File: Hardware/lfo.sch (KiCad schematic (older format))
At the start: 51 parts, among them Q5 2N3904, Q6 2N3904, Q7 2N3904, Q8 2N3904, SW1 SW_DPDT_x2, U4 TL074

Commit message: fix some bias voltage issues in the LFO schematic. Also begin working on envelope firmware, but this is in progress.
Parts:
- added C?: 220uF, Capacitors_SMD:CP_Elec_8x10, symbol CP1
- added R?: 100k, digikey-footprints:0805, symbol R
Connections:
- net GND: now also R?.2
- net lfo_square: now also R?.1
- net at R75.1, R76.2, U4.1: now also C?.1; no longer R78.2
- new net: C?.2, R78.2
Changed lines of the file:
@@
 	3000 3100 2750 3100
 Wire Wire Line
-	2750 3600 2750 3100
+	2750 3100 2750 3600
 Connection ~ 2750 3600
 Wire Wire Line
 	2700 3850 2700 3800
 Wire Wire Line
-	1900 2100 1900 4250
+	1900 3050 1900 4250
 Wire Wire Line
 	1900 4250 1600 4250
@@
 Wire Wire Line
 	2300 2100 2300 2200
-Text Label 2500 2600 0    60   ~ 0
+Text Label 2700 2600 0    60   ~ 0
 lfo_square
 Wire Wire Line
-	2500 2600 2300 2600
+	2300 2600 2700 2600
 Connection ~ 2300 2600
 Text Label 4250 3700 0    60   ~ 0
@@
 	1    0    0    1
 $EndComp
+$Comp
+L R R?
+U 1 1 5C50BA99
+P 2550 2850
+F 0 "R?" V 2630 2850 50  0000 C CNN
+F 1 "100k" V 2550 2850 50  0000 C CNN
+F 2 "digikey-footprints:0805" V 2480 2850 50  0001 C CNN
+F 3 "" H 2550 2850 50  0001 C CNN
+	1    2550 2850
+	1    0    0    -1
+$EndComp
+Wire Wire Line
+	2550 2700 2550 2700
+Wire Wire Line
+	2550 2700 2550 2600
+Connection ~ 2550 2600
+$Comp
+L GND #PWR?
+U 1 1 5C50BC49
+P 2550 3000
+F 0 "#PWR?" H 2550 2750 50  0001 C CNN
+F 1 "GND" H 2550 2850 50  0000 C CNN
+F 2 "" H 2550 3000 50  0001 C CNN
+F 3 "" H 2550 3000 50  0001 C CNN
+	1    2550 3000
+	-1   0    0    -1
+$EndComp
+$Comp
+L CP1 C?
+U 1 1 5C50BEF7
+P 1900 2900
+F 0 "C?" H 1925 3000 50  0000 L CNN
+F 1 "220uF" H 1925 2800 50  0000 L CNN
+F 2 "Capacitors_SMD:CP_Elec_8x10" H 1900 2900 50  0001 C CNN
+F 3 "" H 1900 2900 50  0001 C CNN
+	1    1900 2900
+	-1   0    0    1
+$EndComp
+Wire Wire Line
+	1900 2750 1900 2100
 $EndSCHEMATC

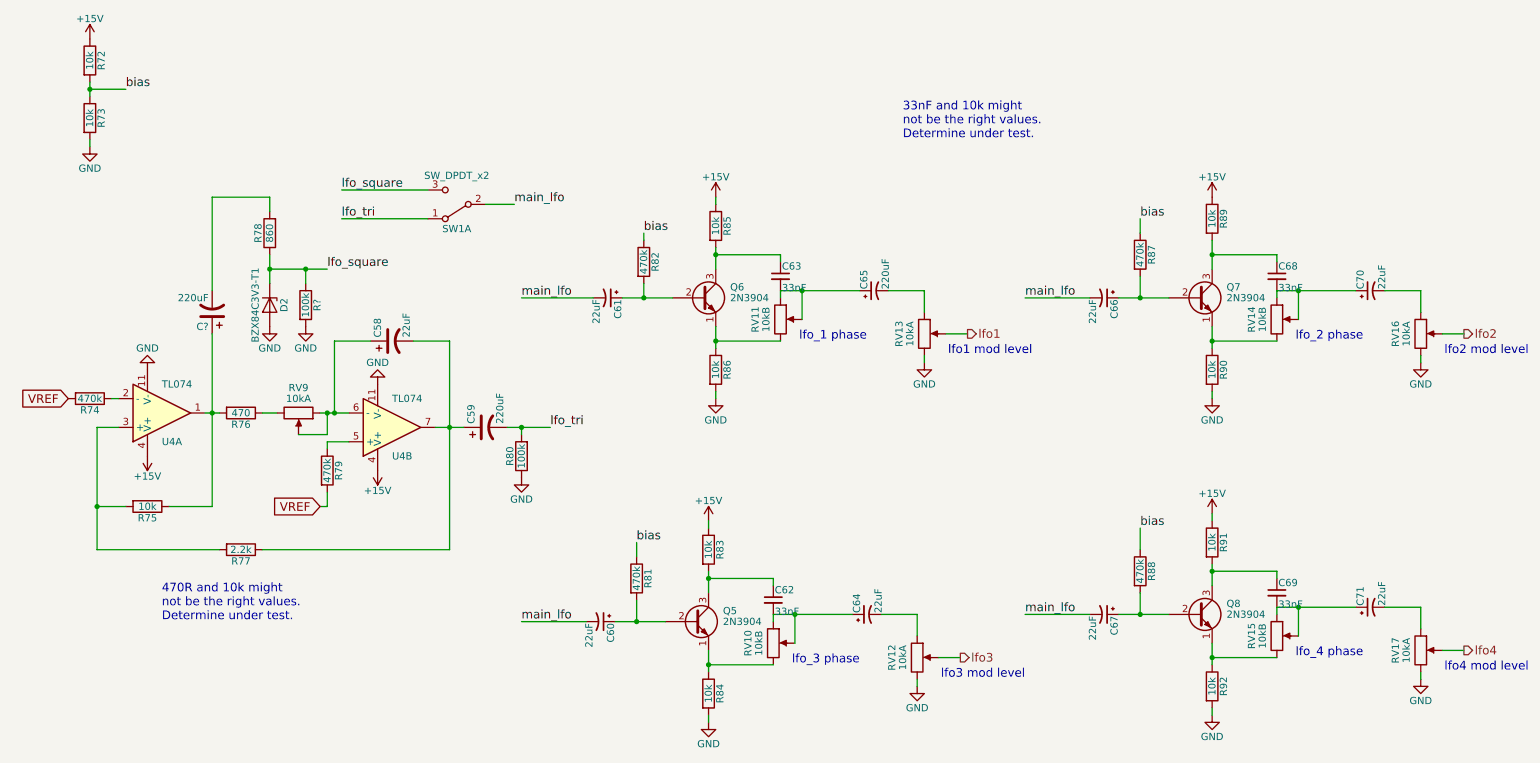
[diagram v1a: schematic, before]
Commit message: change 3.3V to 5V, fix LFO biasing, LPF, JFET bias trim pots.
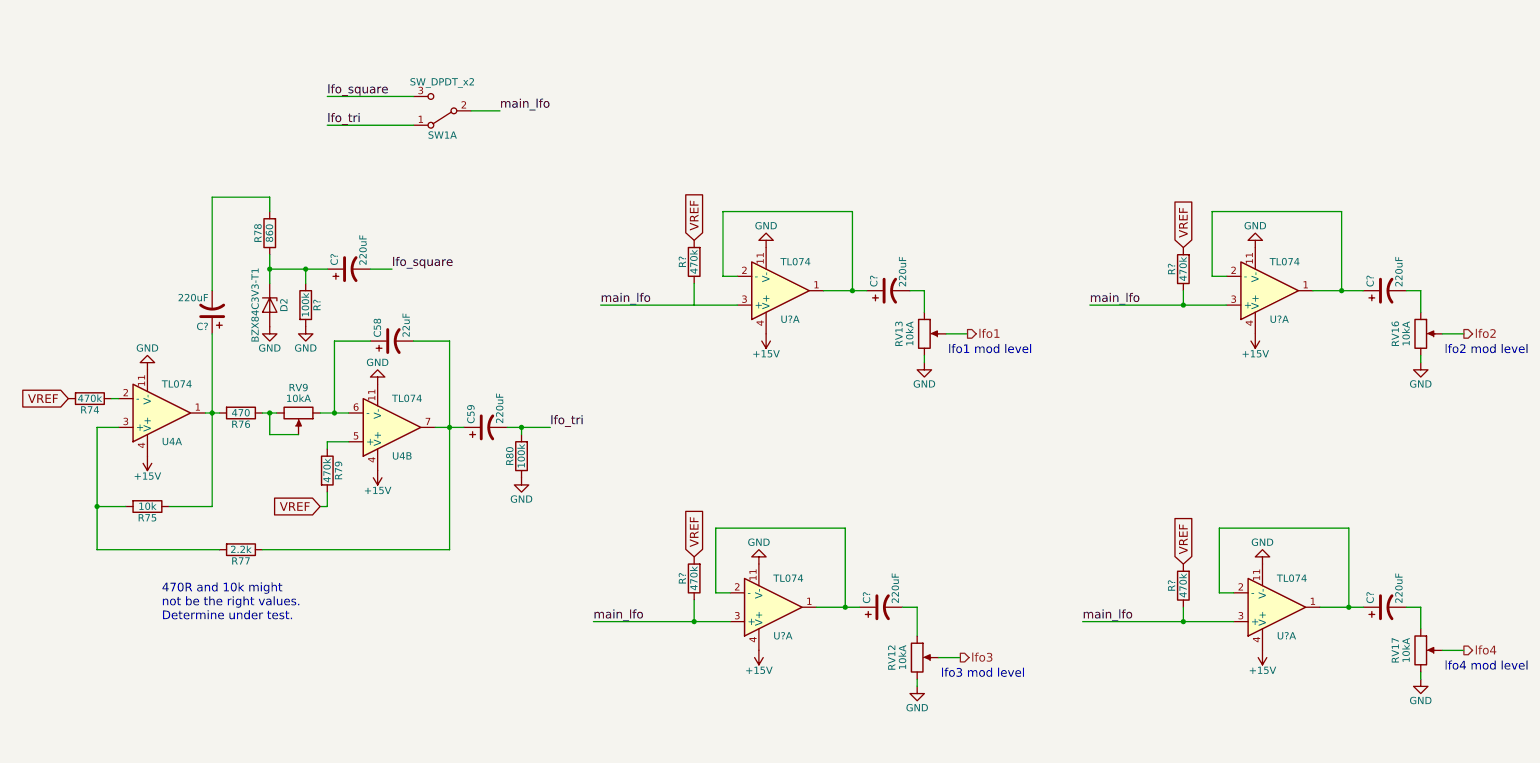
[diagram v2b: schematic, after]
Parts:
- removed C60, C61, C64, C66, C67, C70, C71: 22uF, Capacitors_SMD:CP_Elec_5x5.7, symbol CP1_Small
- removed C62, C63, C68, C69: 33nF, digikey-footprints:0805, symbol C_Small
- removed C65: 220uF, Capacitors_SMD:CP_Elec_8x10, symbol CP1_Small
- removed Q5, Q6, Q7, Q8: 2N3904, digikey-footprints:SOT-23-3, symbol 2N3904
- removed R72, R73, R83, R84, R85, R86, R89, R90, R91, R92: 10k, digikey-footprints:0805, symbol R
- removed R81, R82, R87, R88: 470k, digikey-footprints:0805, symbol R
- removed RV10, RV11, RV14, RV15: 10kB, Potentiometers:Potentiometer_Bourns_PTV09A-1_Horizontal, symbol POT
- added C? (x5): 220uF, Capacitors_SMD:CP_Elec_8x10, symbol CP1
- added R? (x4): 470k, digikey-footprints:0805, symbol R
- added U? (x4): TL074, digikey-footprints:SOIC-14_W3.9mm, symbol TL074
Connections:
- net +15V: now also U?.4 (V+), U?.4 (V+), U?.4 (V+), U?.4 (V+)
- net GND: now also U?.11 (V-), U?.11 (V-), U?.11 (V-), U?.11 (V-)
- net VREF: now also R?.2, R?.2, R?.2, R?.2
- net lfo_square: now also C?.2; no longer D2.1 (K), R78.1, R?.1
- net main_lfo: now also R?.1, R?.1, R?.1, U?.3 (+), U?.3 (+), U?.3 (+), U?.3 (+)
- net at RV13.1: now also C?.2
- net at RV16.1: now also C?.2
- net at RV12.1: now also C?.2
- net at RV17.1: now also C?.2
- net at R76.1, RV9.3: now also RV9.2
- net at C58.1, RV9.1, U4.6 (-): no longer RV9.2
- new net: C?.1, D2.1 (K), R78.1, R?.1
- new net: C?.1, U?.1, U?.2 (-) (x4)
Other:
- note removed: "33nF and 10k might \nnot be the right values.\nDetermine under test."
- note removed: "lfo_1 phase"
- note removed: "lfo_2 phase"
- note removed: "lfo_3 phase"
- note removed: "lfo_4 phase"
- moved on the sheet: SW1A

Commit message: begin PCB v2 layout. fix ref designators, associate footprints on new components, create new PCB file, import components.
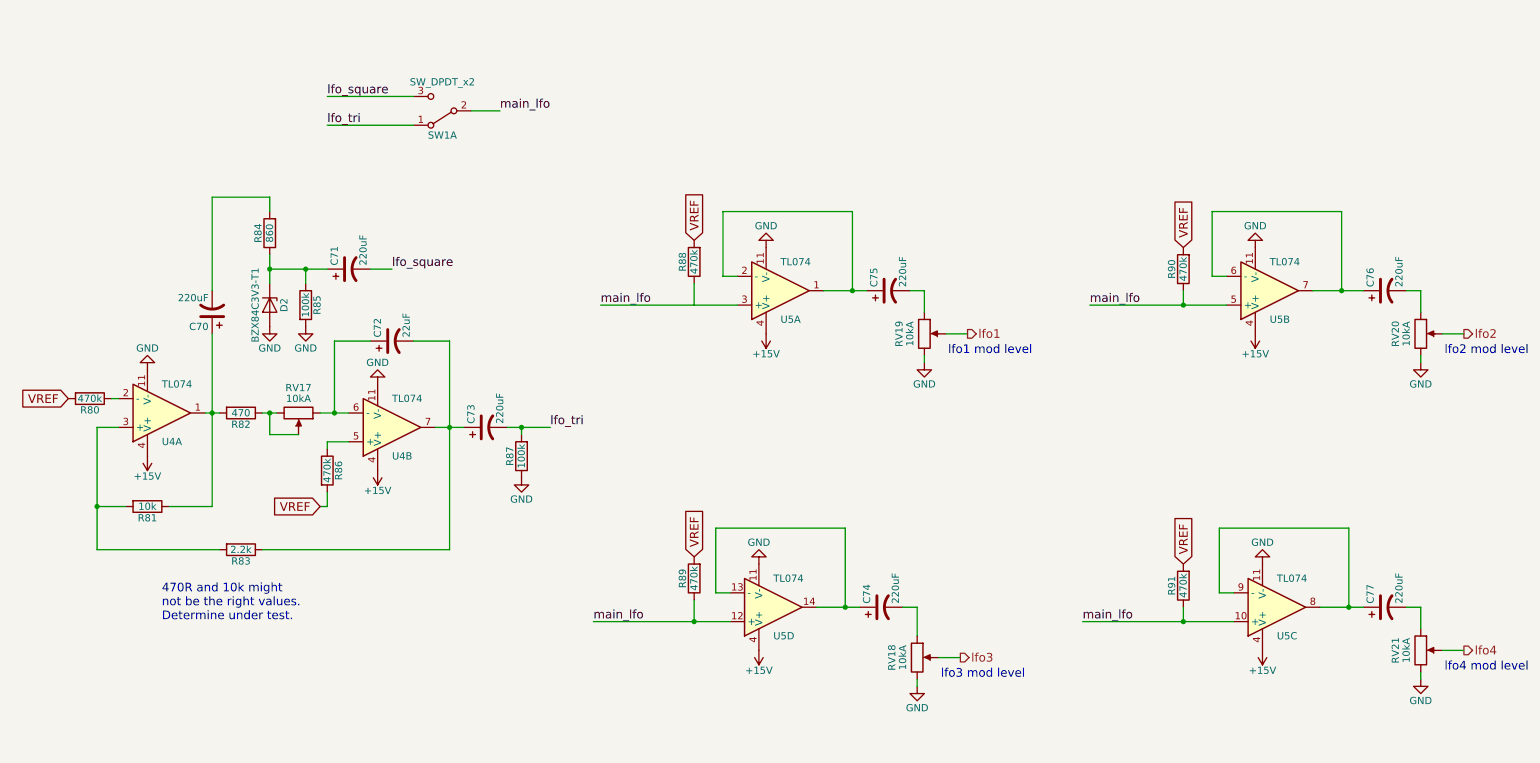
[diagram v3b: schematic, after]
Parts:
- gave numbers to parts that had none: 12
- renumbered C58 to C72, C59 to C73, R74 to R80, R75 to R81, R76 to R82, R77 to R83, R78 to R84, R79 to R86, R80 to R87, RV9 to RV17, RV12 to RV18, RV13 to RV19, RV16 to RV20, RV17 to RV21
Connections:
- net main_lfo: now also U5.10 (+), U5.12 (+), U5.5 (+); no longer U5.3 (+), U5.3 (+), U5.3 (+)
- new net: C76.1, U5.6 (-), U5.7
- new net: C74.1, U5.13 (-), U5.14
- new net: C77.1, U5.8, U5.9 (-)
